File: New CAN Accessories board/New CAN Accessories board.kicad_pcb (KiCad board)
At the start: 2 copper layers, 106 x 91 mm, 101 parts, among them J1 39301040, J10 39301040, J11 ATF13-2P-BM03, J12 Conn_01x02_Pin, J2 39301040, J3 39301040, J4 39301040, J5 39301040, J6 39301040, J7 39301040, J8 39301040, J9 39301060, Q1 IRLML6344TRPBF, Q2 IRLML6344TRPBF, Q3 IRLML6344TRPBF, Q4 IRLML6344TRPBF, Q5 IRLML6344TRPBF, Q6 IRLML6344TRPBF, Q7 IRLML6344TRPBF, Q8 IRLML6344TRPBF, T1 MCP2562FD-E_SN, U1 NUCLEO_L432KC

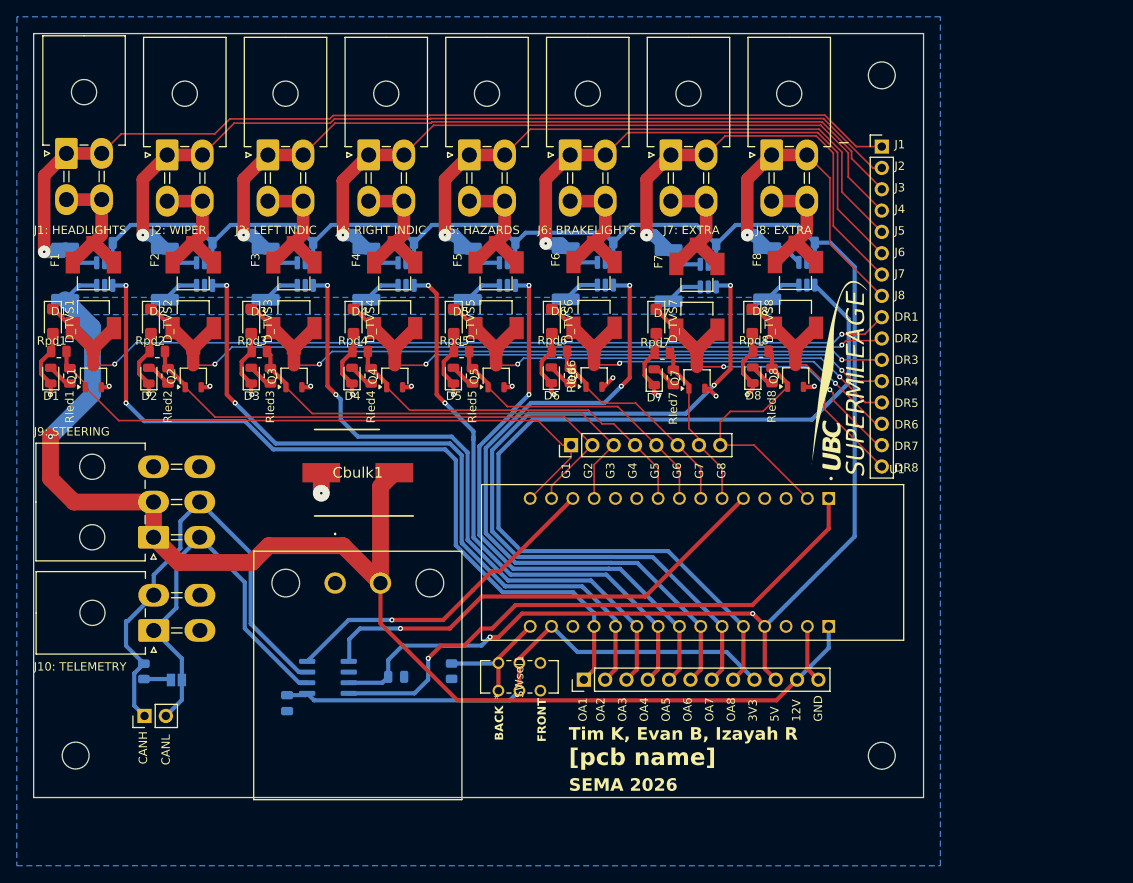
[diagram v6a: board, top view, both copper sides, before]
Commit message: Silk screen fixes
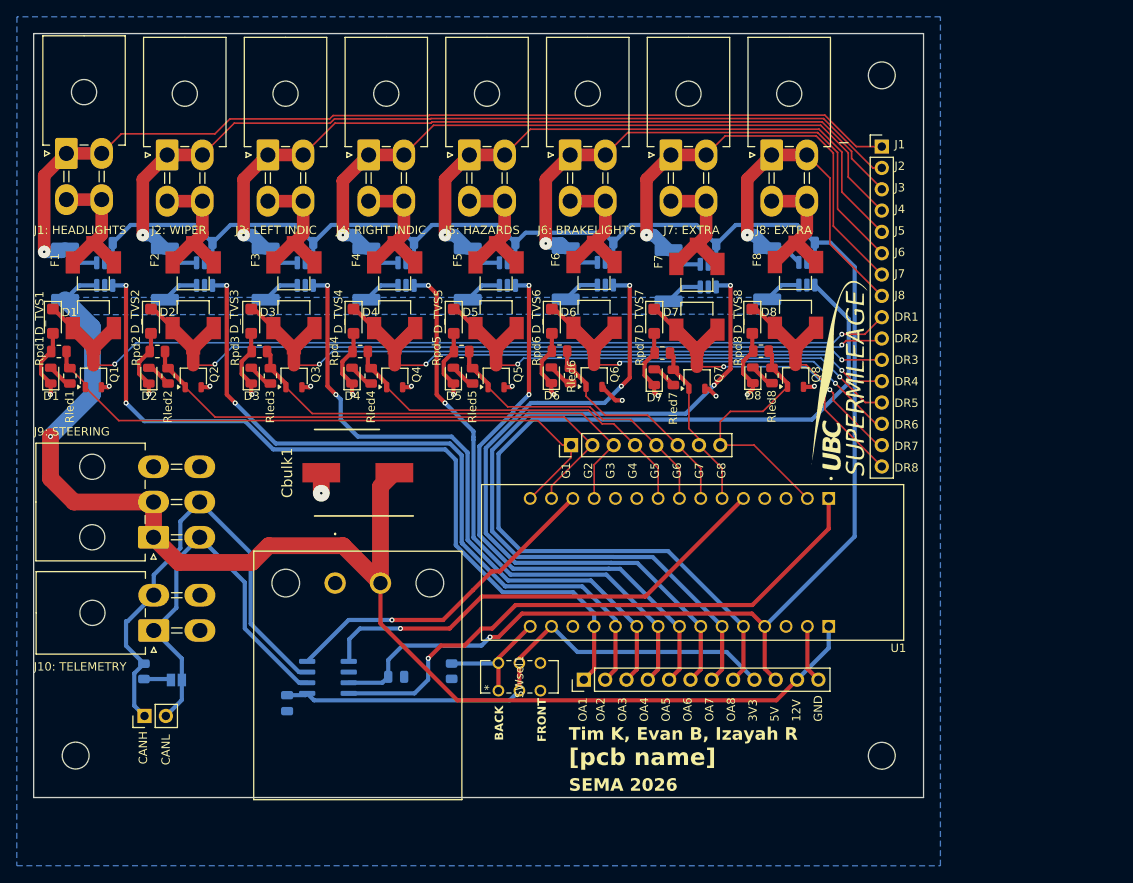
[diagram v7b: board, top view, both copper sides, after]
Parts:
- moved D_TVS7 0.25 mm to (89.9, 50.3)
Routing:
- net GND: track 86.8 -> 88.6 mm
- net /GATE6: track 26.5 -> 27.1 mm
- net 5V: vias 2 -> 1
